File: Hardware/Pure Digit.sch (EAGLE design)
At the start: 44 parts, among them IC1 BA178M05FP, IC3 TL074, IC4 ATMEGA328P, IC5 MCP3202, IC6 MCP4921, Q1 20MHz, SW1 ROTARTY_ENCODER

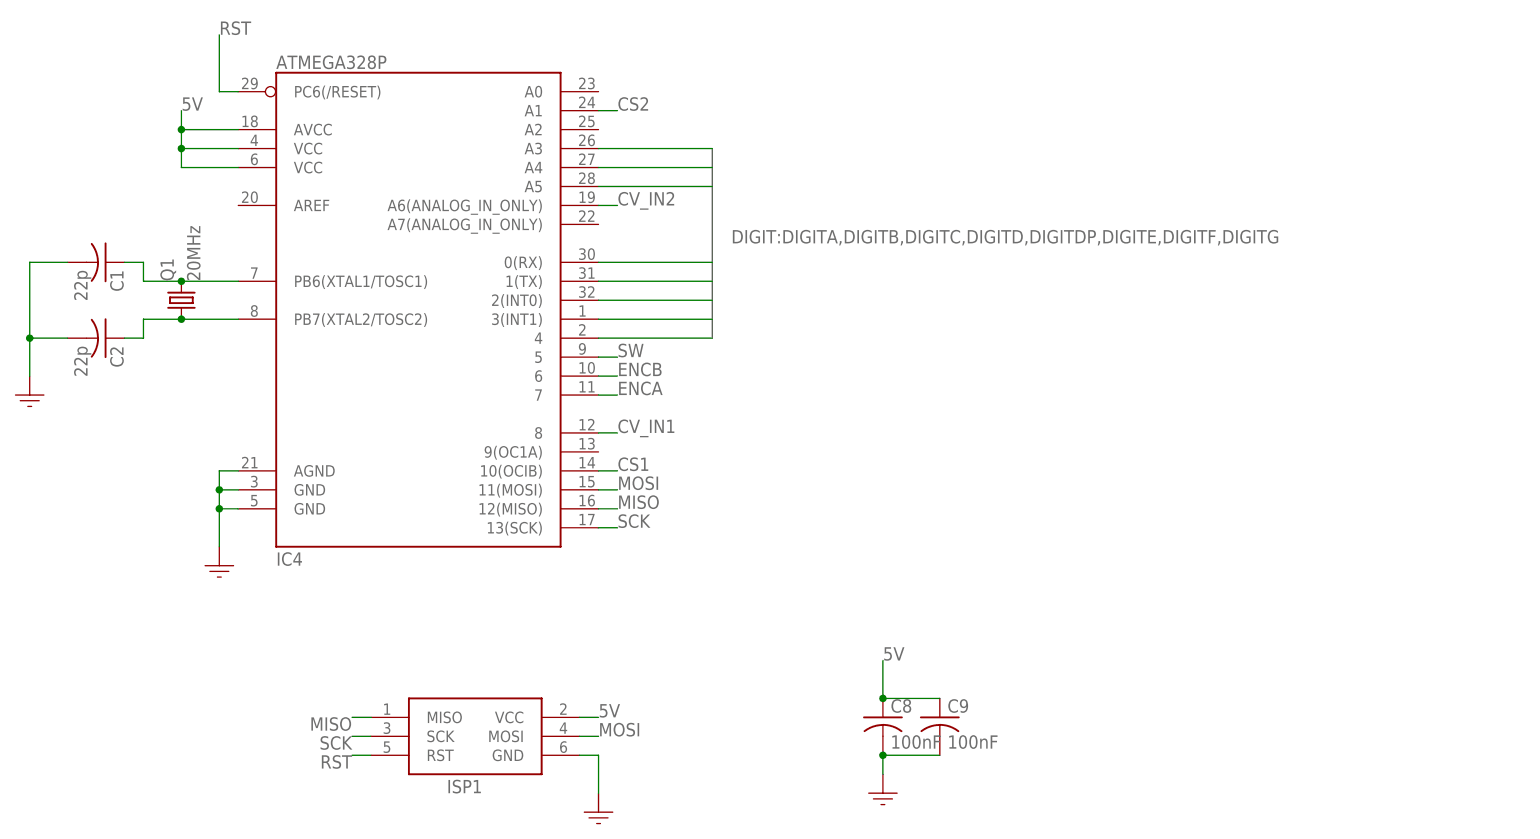
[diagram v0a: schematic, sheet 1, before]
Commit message: Digit 2.0
Digit Updated to V2.0 28/4/21

RC filter added to DAC output.
Cap added to output opamp.
SD Card Reader added.

To do: Replace power so 5V comes from case power supply, inline with low noise techniques. May require complete redesign.
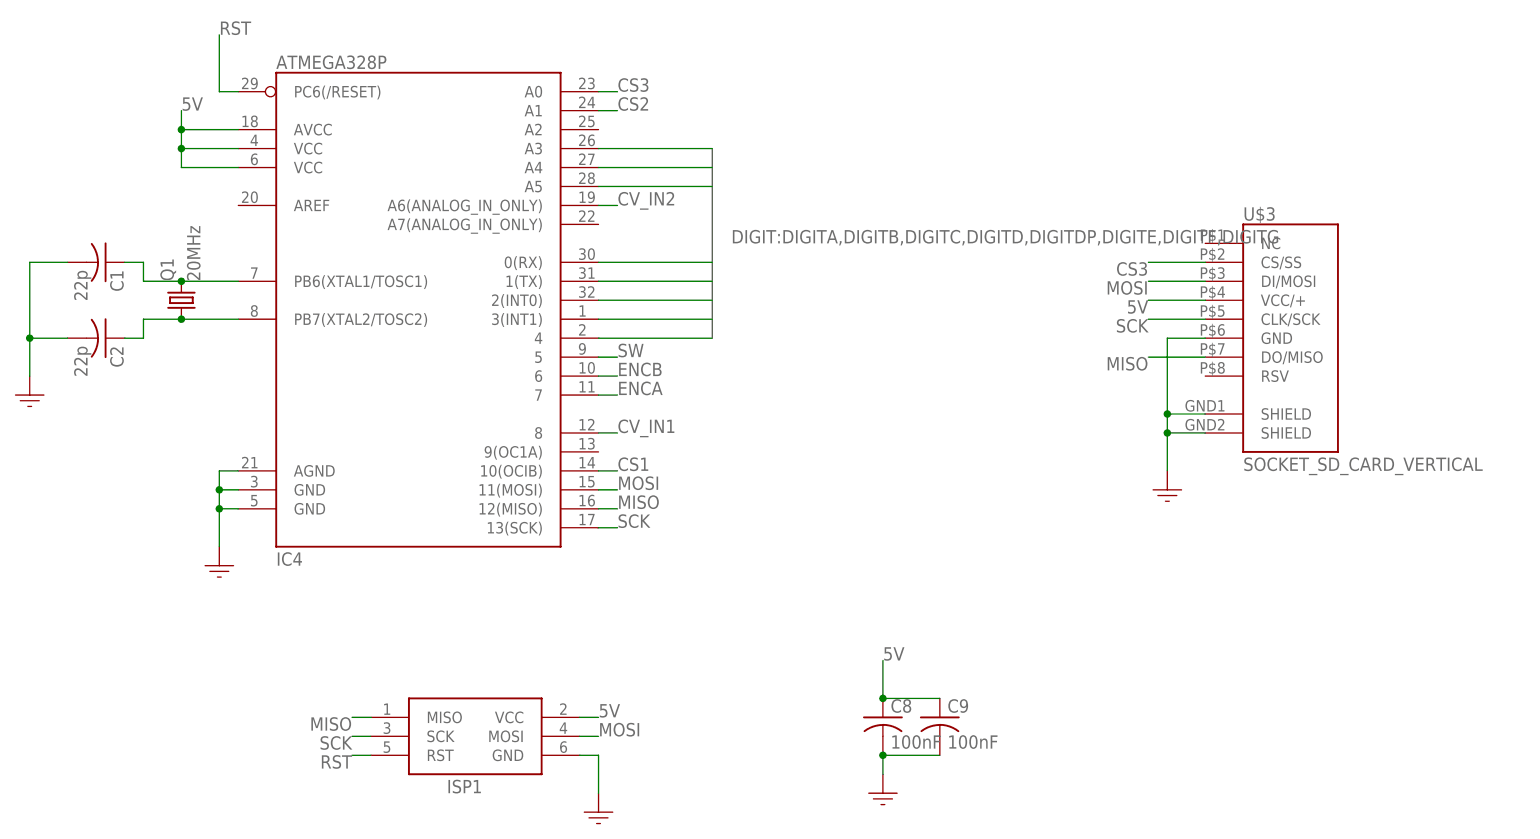
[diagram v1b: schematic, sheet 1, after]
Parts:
- added U$3: SOCKET_SD_CARD_VERTICAL, GMSN:SOCKET_SD_CARD_VERTICAL
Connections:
- new net CS3: IC4.A0, U$3.CS/SS
- net 5V: now also U$3.VCC/+
- net GND: now also U$3.GND, U$3.SHIELD@1, U$3.SHIELD@2
- net MISO: now also U$3.DO/MISO
- net MOSI: now also U$3.DI/MOSI
- net SCK: now also U$3.CLK/SCK
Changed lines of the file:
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@@
 <part name="C14" library="GMSN" library_urn="urn:adsk.eagle:library:27425118" deviceset="CAPACITOR-US" device="C0805" package3d_urn="urn:adsk.eagle:package:27425887/2" value="100nF"/>
 <part name="GND20" library="GMSN" library_urn="urn:adsk.eagle:library:27425118" deviceset="GND" device=""/>
+<part name="U$3" library="GMSN" library_urn="urn:adsk.eagle:library:27425118" deviceset="SOCKET_SD_CARD_VERTICAL" device=""/>
+<part name="GND21" library="GMSN" library_urn="urn:adsk.eagle:library:27425118" deviceset="GND" device=""/>
 </parts>
 <sheets>
@@
 <attribute name="VALUE" x="128.016" y="69.469" size="1.778" layer="96"/>
 </instance>
+<instance part="U$3" gate="G$1" x="170.18" y="124.46" smashed="yes">
+<attribute name="NAME" x="167.64" y="140.208" size="1.778" layer="95"/>
+<attribute name="VALUE" x="167.64" y="106.68" size="1.778" layer="96"/>
+</instance>
+<instance part="GND21" gate="1" x="157.48" y="106.68" smashed="yes" rot="MR0"/>
 </instances>
 <busses>
@@
 <pinref part="GND15" gate="1" pin="GND"/>
 </segment>
+<segment>
+<pinref part="U$3" gate="G$1" pin="GND"/>
+<wire x1="162.56" y1="124.46" x2="157.48" y2="124.46" width="0.1524" layer="91"/>
+<pinref part="U$3" gate="G$1" pin="SHIELD@1"/>
+<wire x1="162.56" y1="114.3" x2="157.48" y2="114.3" width="0.1524" layer="91"/>
+<wire x1="157.48" y1="114.3" x2="157.48" y2="111.76" width="0.1524" layer="91"/>
+<pinref part="U$3" gate="G$1" pin="SHIELD@2"/>
+<wire x1="157.48" y1="111.76" x2="157.48" y2="106.68" width="0.1524" layer="91"/>
+<wire x1="162.56" y1="111.76" x2="157.48" y2="111.76" width="0.1524" layer="91"/>
+<junction x="157.48" y="111.76"/>
+<wire x1="157.48" y1="124.46" x2="157.48" y2="114.3" width="0.1524" layer="91"/>
+<junction x="157.48" y="114.3"/>
+<pinref part="GND21" gate="1" pin="GND"/>
+</segment>
 </net>
 <net name="RST" class="0">
@@
 <label x="83.82" y="101.6" size="1.778" layer="95"/>
 </segment>
+<segment>
+<pinref part="U$3" gate="G$1" pin="DO/MISO"/>
+<wire x1="162.56" y1="121.92" x2="154.94" y2="121.92" width="0.1524" layer="91"/>
+<label x="154.94" y="121.92" size="1.778" layer="95" rot="R180"/>
+</segment>
 </net>
 <net name="SCK" class="0">
@@
 <label x="83.82" y="99.06" size="1.778" layer="95"/>
 </segment>
+<segment>
+<pinref part="U$3" gate="G$1" pin="CLK/SCK"/>
+<wire x1="162.56" y1="127" x2="154.94" y2="127" width="0.1524" layer="91"/>
+<label x="154.94" y="127" size="1.778" layer="95" rot="R180"/>
+</segment>
 </net>
 <net name="MOSI" class="0">
@@
 <wire x1="81.28" y1="104.14" x2="83.82" y2="104.14" width="0.1524" layer="91"/>
 <label x="83.82" y="104.14" size="1.778" layer="95"/>
+</segment>
+<segment>
+<pinref part="U$3" gate="G$1" pin="DI/MOSI"/>
+<wire x1="162.56" y1="132.08" x2="154.94" y2="132.08" width="0.1524" layer="91"/>
+<label x="154.94" y="132.08" size="1.778" layer="95" rot="R180"/>
 </segment>
 </net>
@@
 <pinref part="C9" gate="G$1" pin="1"/>
 </segment>
+<segment>
+<pinref part="U$3" gate="G$1" pin="VCC/+"/>
+<wire x1="162.56" y1="129.54" x2="154.94" y2="129.54" width="0.1524" layer="91"/>
+<label x="154.94" y="129.54" size="1.778" layer="95" rot="R180"/>
+</segment>
 </net>
 <net name="DIGITDP" class="0">
@@
 <wire x1="81.28" y1="111.76" x2="83.82" y2="111.76" width="0.1524" layer="91"/>
 <label x="83.82" y="111.76" size="1.778" layer="95"/>
+</segment>
+</net>
+<net name="CS3" class="0">
+<segment>
+<pinref part="U$3" gate="G$1" pin="CS/SS"/>
+<wire x1="162.56" y1="134.62" x2="154.94" y2="134.62" width="0.1524" layer="91"/>
+<label x="154.94" y="134.62" size="1.778" layer="95" rot="R180"/>
+</segment>
+<segment>
+<pinref part="IC4" gate="G$1" pin="A0"/>
+<wire x1="81.28" y1="157.48" x2="83.82" y2="157.48" width="0.1524" layer="91"/>
+<label x="83.82" y="157.48" size="1.778" layer="95"/>
 </segment>
 </net>
@@
 </sheet>
 </sheets>
+<errors>
+</errors>
 </schematic>
 </drawing>
